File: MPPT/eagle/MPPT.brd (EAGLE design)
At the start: 1 part, among them U1 STM32F042K6

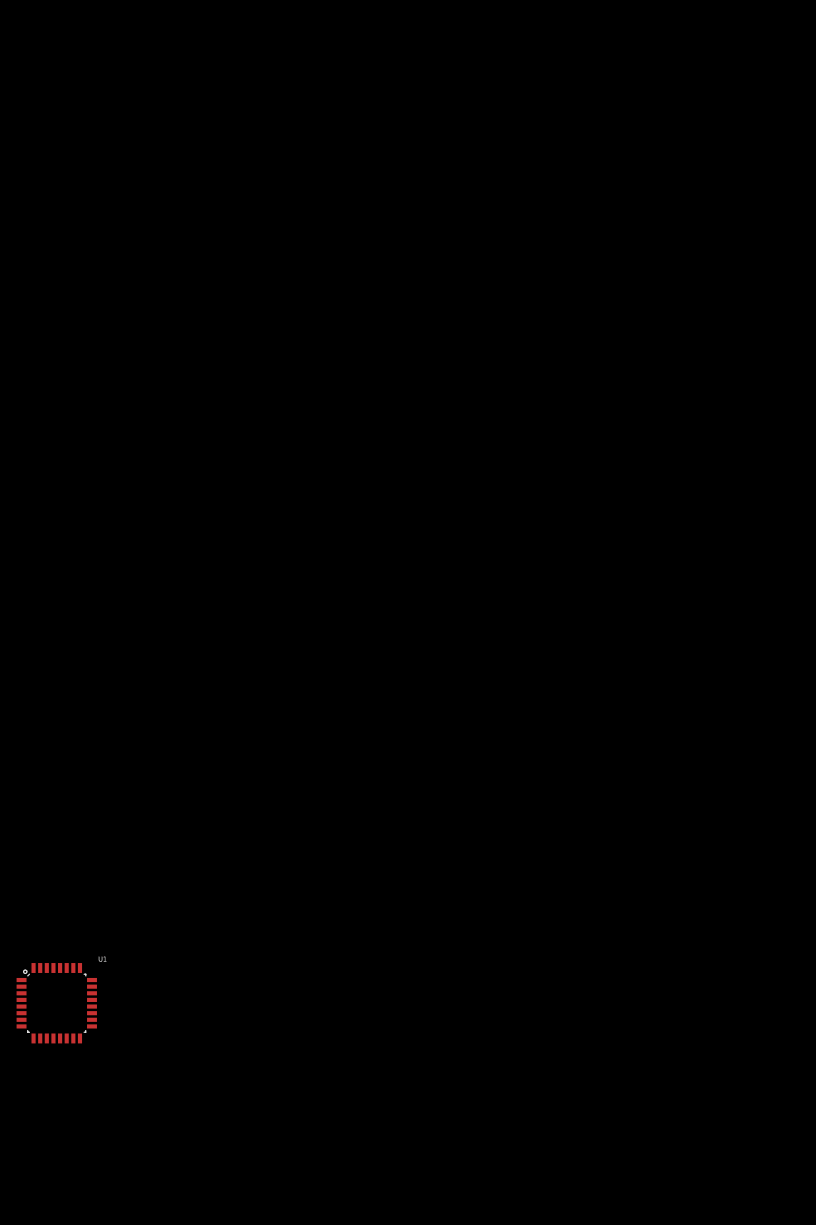
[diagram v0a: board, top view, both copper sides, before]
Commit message: Added Components for MPPT, started MPPT .brd .sch add TCAN330
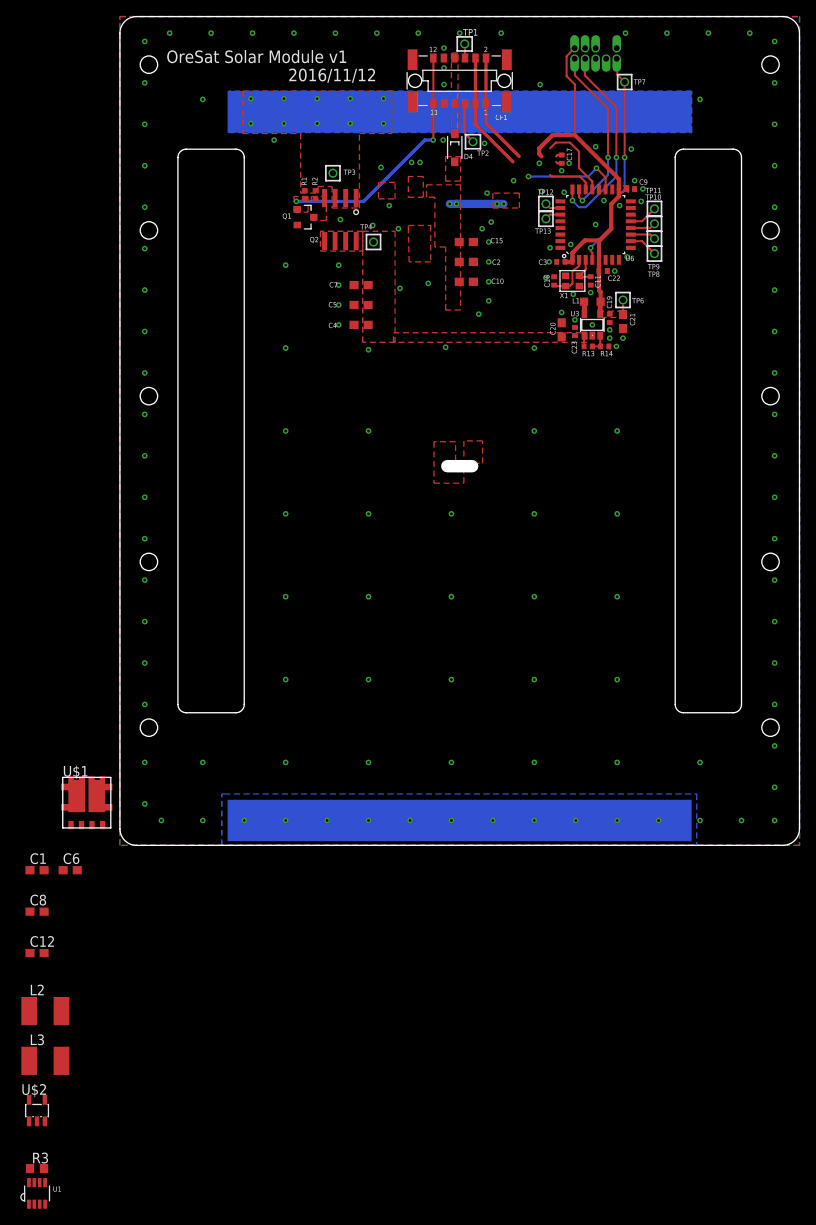
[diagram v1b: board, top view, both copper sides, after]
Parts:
- added C1, C10, C12, C2, C4, C5, C6, C7, C8: NP, rcl_custom:C0603
- added C11, C16: 20p?, rcl_custom:.0402-B-NOSILK
- added C15: 47u, rcl_custom:C0603
- added C17, C19, C22, C23, C3, C9: 100n, rcl_custom:.0402-B-NOSILK
- added C20, C21: 4.7u, rcl:C0603
- added CF1: ORESAT-SOLARPANEL-12PIN, oresat-eagle:CON-1.27-F-HARTING-1522012X601XXX
- added D2: ALTA-5-CELL-ARRAY, alta-cell:ALTA-FIVE-CELL
- added D4: SOD123-B SCHOTTKY, apdm:SOD123-B
- added J1: 1.27MM-SWD-CONNECTOR, con-swd:1.27MM_2X5
- added L1: 10u, rcl:L2012C
- added L2, L3: (no value), rcl:L1812
- added Q1: ON-NFET, on-n-channel-fet:SOT23
- added Q2: P-CHANNELFET, vishay-p-channel-fet:SO8
- added R1: 10k, rcl_custom:.0402-B-NOSILK
- added R13, R2: 100k, rcl_custom:.0402-B-NOSILK
- added R14: 33.3k, rcl_custom:.0402-B-NOSILK
- added R3: (no value), rcl:R0603
- added TP1, TP10, TP11, TP12, TP13, TP2, TP3, TP4, TP6, TP7, TP8, TP9: TEST-POINT, Tova:2MM-TEST-POINT
- added U$1: N-PMOSFET, N-PMosfet:5X6POWERFLAT
- added U$2: TSC888, TSC888:SOT23-5
- added U3: LM3671MF-3.3, LM3761:SOT23-5
- added U6: STM32F042K6, STM32F042K:QFP32-7X7
- added X1: 8MHZ-2.5x2mm, low-gain-radio:CRYSTAL_2.5X2
- U1: value STM32F042K6 -> TCAN330; device STM32F042K:QFP32-7X7 -> TCAN330:SOT23-8_TI-DCN
- moved U1 23.1 mm to (-10.0, -42.0)
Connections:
- removed net VDD: U1.1
- removed net VDDA: U1.5
- removed net VDDIO2: U1.17
- removed net VSS: U1.16, U1.32
- new net 3.3V: C17.2, C19.1, C21.1, C22.2, C3.2, C9.2, J1.VTREF, L1.1, TP6.1, U$2.5, U1.3, U3.4, U6.1, U6.17, U6.5
- new net CANH: CF1.3, CF1.4, U1.7
- new net CANL: CF1.1, CF1.2, U1.6
- new net CAN_ENABLE: U1.5, U6.20
- new net CAN_LSTN: U1.8, U6.19
- new net CAN_RX: U1.4, U6.21
- new net CAN_TX: U1.1, U6.22
- new net CRYSTALIN: C16.1, U6.2, X1.1
- new net CRYSTALOUT: C11.1, U6.3, X1.3
- new net GND: C10.2, C11.2, C15.2, C16.2, C17.1, C19.2, C2.2, C20.2, C21.2, C22.1, C23.2, C3.1, C4.2, C5.2, C7.2, C9.1, CF1.10, CF1.9, D2.NEG, J1.GND, J1.GND@2, J1.GNDDET, L2.2, Q1.2, R14.1, U$1.S2, U$2.2, U1.2, U3.2, U6.16, U6.32, X1.2, X1.4
- new net N$1: C1.1, C12.1, C6.1, C8.1, L2.1, U$1.D1, U$1.D11, U$1.D12, U$1.D13, U$1.D14
- new net N$10: TP13.1, U6.27
- new net N$11: C10.1, C15.1, C2.1, L3.1, R3.1, U$2.4
- new net N$12: U$1.G1, U6.7
- new net N$14: D4.A, R3.2, U$2.3
- new net N$2: C1.2, C12.2, C6.2, C8.2, L3.2, U$1.D2, U$1.D21, U$1.D22, U$1.D23, U$1.D24
- new net N$3: CF1.6, TP1.1
- new net N$4: CF1.5, TP2.1
- new net N$5: TP8.1, U6.10
- new net N$6: TP9.1, U6.11
- new net N$7: TP10.1, U$2.1, U6.12
- new net N$8: TP11.1, U$1.G2, U6.13
- new net N$9: TP12.1, U6.26
- new net N6: Q1.3, Q2.4, R2.1
- new net ORESAT-SHDN: CF1.11, CF1.12, Q1.1, R1.1
- new net RESET: J1.!RESET, TP7.1, U6.4
- new net SOLAR-IN: D2.POS, Q2.1, Q2.2, Q2.3, R1.2, R2.2, TP3.1
- new net SOLAR-IN-SWITCHED: C20.1, C23.1, C4.1, C5.1, C7.1, Q2.5, Q2.6, Q2.7, Q2.8, R13.2, TP4.1, U$1.S1, U3.1
- new net STEPD: L1.2, U3.5
- new net SWCLK: J1.SWDCLK, U6.24
- new net SWDIO: J1.SWDIO, U6.23
- new net VDIV: R13.1, R14.2, U3.3
- new net VPV: CF1.7, CF1.8, D4.K
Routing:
- net 3.3V: track 0.00 -> 50.6 mm
- net ORESAT-SHDN: track 0.00 -> 29.5 mm, vias 0 -> 2
- net RESET: track 0.00 -> 26.4 mm, vias 0 -> 2
- net SWCLK: track 0.00 -> 24.3 mm, vias 0 -> 2
- net SWDIO: track 0.00 -> 21.6 mm, vias 0 -> 2
- net CANH: track 0.00 -> 14.4 mm
- net CANL: track 0.00 -> 13.5 mm
- net CAN_LSTN: track 0.00 -> 11.6 mm, vias 0 -> 2
- net CAN_RX: track 0.00 -> 9.46 mm
- net SOLAR-IN-SWITCHED2: track 0.00 -> 6.50 mm, vias 0 -> 4
- net CRYSTALIN: track 0.00 -> 5.64 mm
- net CAN_TX: track 0.00 -> 5.52 mm
- net N$4: track 0.00 -> 5.00 mm
- net CRYSTALOUT: track 0.00 -> 3.67 mm
- net N$8: track 0.00 -> 3.47 mm
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- added copper zone on layer 1, net 3.3V
- added copper zone on layer 1, net GND
- added copper zone on layer 16, net GND
- added copper zone on layer 1, net N6
- added copper zone on layer 1, net ORESAT-SHDN
- added copper zone on layer 1, net SOLAR-IN
- added copper zone on layer 16, net SOLAR-IN
- added copper zone on layer 1, net SOLAR-IN-SWITCHED
- added copper zone on layer 1, net SOLAR-IN-SWITCHED2
- added copper zone on layer 1, net V3
- added copper zone on layer 1, net V4
- added copper zone on layer 1, net VCTRL
- added copper zone on layer 1, net VOUT
- added copper zone on layer 1, net VPV
- added copper zone on layer 1, net VSOLAR
- added copper zone on layer 1, net XSHUT
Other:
- board outline added: 82 x 100 mm
- board text added: "2016/11/12"
- board text added: "OreSat Solar Module v1"

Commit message: Added attributes to remaining parts.
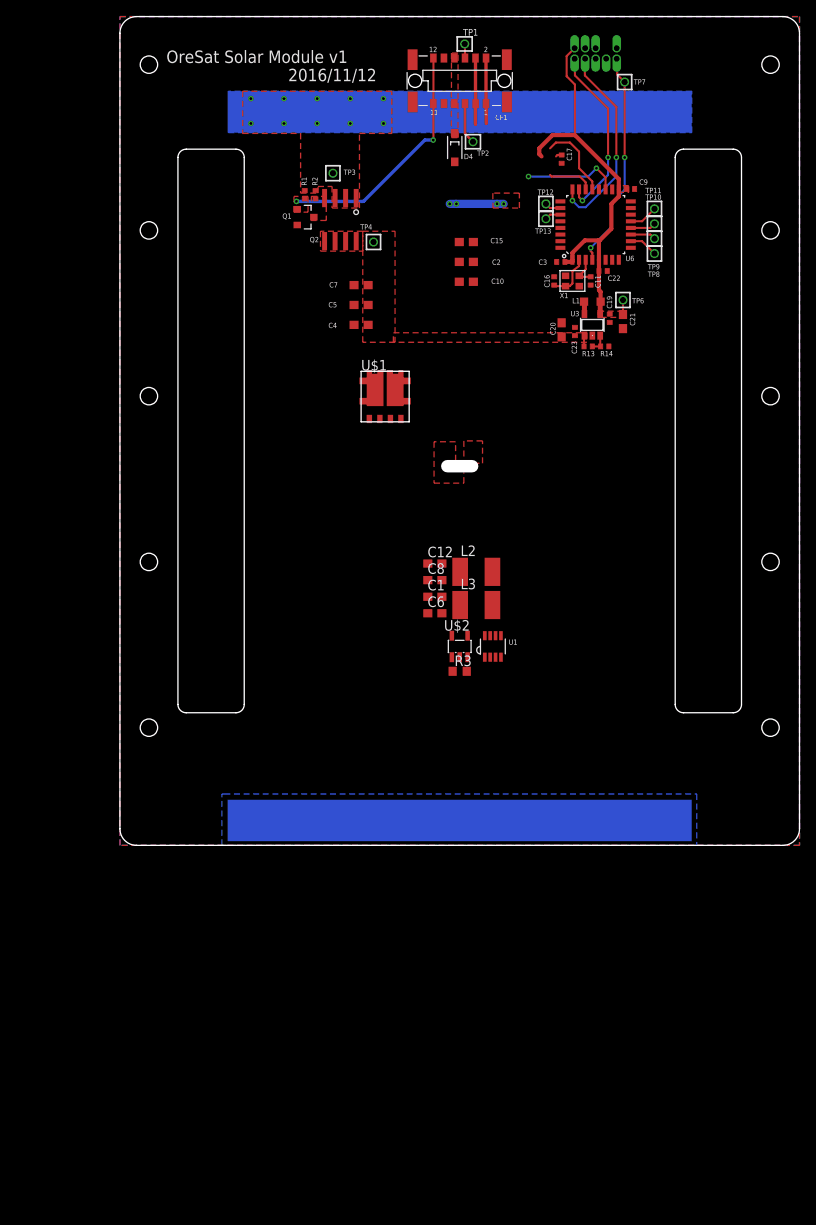
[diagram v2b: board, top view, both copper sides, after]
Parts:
- moved U1 85.9 mm to (45.0, 24.0)
- moved R3 78.7 mm to (41.0, 21.0)
- moved U$2 75.7 mm to (41.0, 24.0)
- moved L3 75.7 mm to (43.0, 29.0)
- moved L2 74.2 mm to (43.0, 33.0)
- moved C12 67.2 mm to (38.0, 34.0)
- moved C8 62.5 mm to (38.0, 32.0)
- moved U$1 60.8 mm to (32.0, 53.0)
- moved C1 58.2 mm to (38.0, 30.0)
- moved C6 53.8 mm to (38.0, 28.0)
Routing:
- net CANH: track 14.4 -> 8.00 mm
- net CANL: track 13.5 -> 7.91 mm
- net GND: track 0.75 -> 0.00 mm, vias 157 -> 0
- removed copper zone on layer 1, net VCTRL
- removed copper zone on layer 1, net VOUT
- removed copper zone on layer 1, net VSOLAR
- removed copper zone on layer 1, net XSHUT
